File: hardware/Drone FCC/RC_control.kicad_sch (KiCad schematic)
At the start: 2 parts, among them J24 DSM Spektrum JST, J27 PPM Dupont

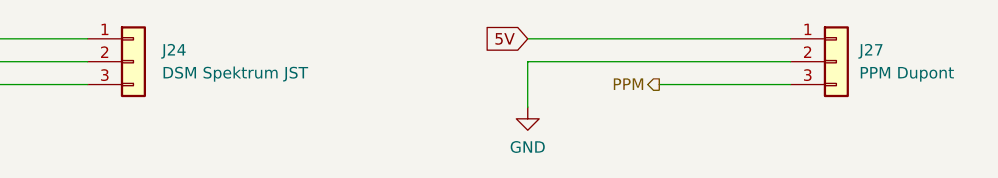
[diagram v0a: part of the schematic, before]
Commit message: re enumeration of components
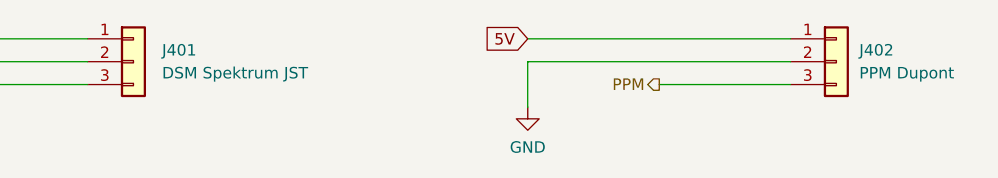
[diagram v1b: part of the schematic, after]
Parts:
- renumbered J24 to J401, J27 to J402
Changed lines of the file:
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@@
   (symbol (lib_id "Connector_Generic:Conn_01x03") (at 83.185 42.545 0) (unit 1)
     (in_bom yes) (on_board yes) (fields_autoplaced)
-    (property "Reference" "J24" (id 0) (at 86.36 41.2749 0)
+    (property "Reference" "J401" (id 0) (at 86.36 41.2749 0)
       (effects (font (size 1.27 1.27)) (justify left))
     )
@@
   (symbol (lib_id "Connector_Generic:Conn_01x03") (at 161.29 42.545 0) (unit 1)
     (in_bom yes) (on_board yes) (fields_autoplaced)
-    (property "Reference" "J27" (id 0) (at 163.83 41.2749 0)
+    (property "Reference" "J402" (id 0) (at 163.83 41.2749 0)
       (effects (font (size 1.27 1.27)) (justify left))
     )

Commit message: start routing
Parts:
- removed J401: DSM Spektrum JST, B3B-ZR-SM4-TF(LF)(SN):JST-B3B-ZR-SM4-TFLFSN-0-0-MFG, symbol Connector_Generic:Conn_01x03
- added J401: DSM Spektrum JST, B3B-ZR-SM4-TF(LF)(SN):JST-B3B-ZR-SM4-TFLFSN-0-0-MFG, symbol Connector_Generic:Conn_01x05
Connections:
- net 3V3: now also J401.1 (Pin_1)
- net DSM_DATA: now also J401.3 (Pin_3)
- net GND: now also J401.2 (Pin_2), J401.4 (Pin_4), J401.5 (Pin_5)
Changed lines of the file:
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@@
 (kicad_sch (version 20211123) (generator eeschema)
   (paper "A4")
+  (junction (at 48.895 50.165) (diameter 0) (color 0 0 0 0)
+  )
+  (junction (at 48.895 47.625) (diameter 0) (color 0 0 0 0)
+  )
+  (wire (pts (xy 48.895 47.625) (xy 48.895 50.165))
+    (stroke (width 0) (type default) (color 0 0 0 0))
+  )
+  (wire (pts (xy 48.895 50.165) (xy 48.895 52.705))
+    (stroke (width 0) (type default) (color 0 0 0 0))
+  )
   (wire (pts (xy 127 42.545) (xy 156.21 42.545))
+    (stroke (width 0) (type default) (color 0 0 0 0))
+  )
+  (wire (pts (xy 48.895 50.165) (xy 78.105 50.165))
     (stroke (width 0) (type default) (color 0 0 0 0))
   )
@@
   )
   (wire (pts (xy 48.895 40.005) (xy 78.105 40.005))
+    (stroke (width 0) (type default) (color 0 0 0 0))
+  )
+  (wire (pts (xy 48.895 47.625) (xy 78.105 47.625))
     (stroke (width 0) (type default) (color 0 0 0 0))
   )
@@
     (effects (font (size 1.27 1.27)) (justify right))
   )
-  (symbol (lib_id "Connector_Generic:Conn_01x03") (at 83.185 42.545 0) (unit 1)
+  (symbol (lib_id "Connector_Generic:Conn_01x05") (at 83.185 45.085 0) (unit 1)
     (in_bom yes) (on_board yes) (fields_autoplaced)
-    (property "Reference" "J401" (id 0) (at 86.36 41.2749 0)
+    (property "Reference" "J401" (id 0) (at 86.36 43.8149 0)
       (effects (font (size 1.27 1.27)) (justify left))
     )
-    (property "Value" "DSM Spektrum JST" (id 1) (at 86.36 43.8149 0)
+    (property "Value" "DSM Spektrum JST" (id 1) (at 86.36 46.3549 0)
       (effects (font (size 1.27 1.27)) (justify left))
     )
-    (property "Footprint" "B3B-ZR-SM4-TF(LF)(SN):JST-B3B-ZR-SM4-TFLFSN-0-0-MFG" (id 2) (at 83.185 42.545 0)
+    (property "Footprint" "B3B-ZR-SM4-TF(LF)(SN):JST-B3B-ZR-SM4-TFLFSN-0-0-MFG" (id 2) (at 83.185 45.085 0)
       (effects (font (size 1.27 1.27)) hide)
     )
-    (property "Datasheet" "~" (id 3) (at 83.185 42.545 0)
+    (property "Datasheet" "~" (id 3) (at 83.185 45.085 0)
       (effects (font (size 1.27 1.27)) hide)
     )
@@
     (pin "2")
     (pin "3")
+    (pin "4")
+    (pin "5")
   )
   (symbol (lib_id "Connector_Generic:Conn_01x03") (at 161.29 42.545 0) (unit 1)
@@
     (pin "1")
   )
-  (symbol (lib_id "power:GND") (at 48.895 47.625 0) (unit 1)
+  (symbol (lib_id "power:GND") (at 48.895 52.705 0) (unit 1)
     (in_bom yes) (on_board yes) (fields_autoplaced)
-    (property "Reference" "#PWR0119" (id 0) (at 48.895 53.975 0)
+    (property "Reference" "#PWR0119" (id 0) (at 48.895 59.055 0)
       (effects (font (size 1.27 1.27)) hide)
     )
-    (property "Value" "GND" (id 1) (at 48.895 52.07 0))
-    (property "Footprint" "" (id 2) (at 48.895 47.625 0)
+    (property "Value" "GND" (id 1) (at 48.895 57.15 0))
+    (property "Footprint" "" (id 2) (at 48.895 52.705 0)
       (effects (font (size 1.27 1.27)) hide)
     )
-    (property "Datasheet" "" (id 3) (at 48.895 47.625 0)
+    (property "Datasheet" "" (id 3) (at 48.895 52.705 0)
       (effects (font (size 1.27 1.27)) hide)
     )

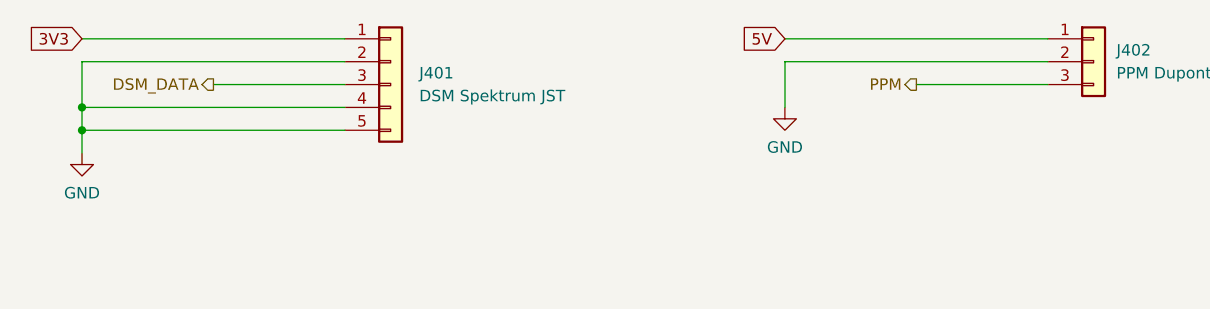
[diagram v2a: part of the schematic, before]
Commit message: add TVS diodes for SPI and ESD capacitors
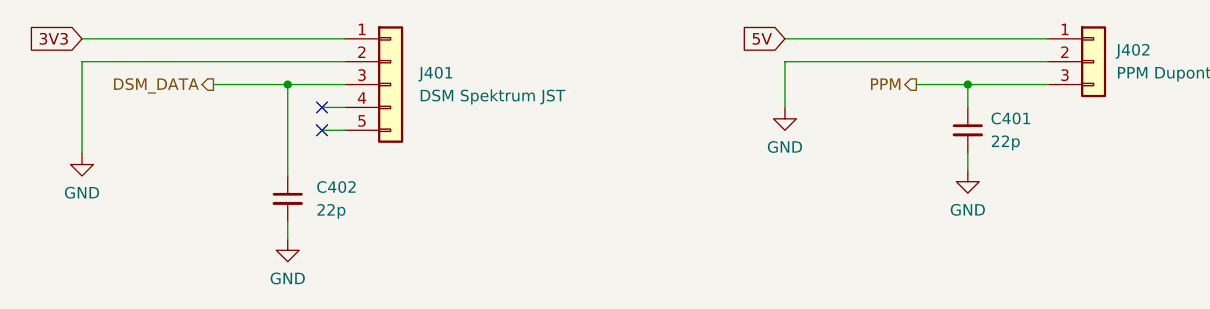
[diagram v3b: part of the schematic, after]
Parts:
- added C401, C402: 22p, Capacitor_SMD:C_0402_1005Metric_Pad0.74x0.62mm_HandSolder, symbol Device:C_Small
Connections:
- net DSM_DATA: now also C402.1
- net GND: now also C401.2, C402.2; no longer J401.4 (Pin_4), J401.5 (Pin_5)
- net PPM: now also C401.1
- no-connect marks 0 -> 2
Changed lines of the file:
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@@
 (kicad_sch (version 20211123) (generator eeschema)
   (paper "A4")
-  (junction (at 48.895 50.165) (diameter 0) (color 0 0 0 0)
-  )
-  (junction (at 48.895 47.625) (diameter 0) (color 0 0 0 0)
-  )
-  (wire (pts (xy 48.895 47.625) (xy 48.895 50.165))
-    (stroke (width 0) (type default) (color 0 0 0 0))
-  )
-  (wire (pts (xy 48.895 50.165) (xy 48.895 52.705))
+  (junction (at 71.755 45.085) (diameter 0) (color 0 0 0 0)
+  )
+  (junction (at 147.32 45.085) (diameter 0) (color 0 0 0 0)
+  )
+  (no_connect (at 75.565 50.165))
+  (no_connect (at 75.565 47.625))
+  (wire (pts (xy 48.895 42.545) (xy 48.895 52.705))
+    (stroke (width 0) (type default) (color 0 0 0 0))
+  )
+  (wire (pts (xy 75.565 50.165) (xy 78.105 50.165))
+    (stroke (width 0) (type default) (color 0 0 0 0))
+  )
+  (wire (pts (xy 147.32 52.705) (xy 147.32 54.61))
     (stroke (width 0) (type default) (color 0 0 0 0))
   )
@@
     (stroke (width 0) (type default) (color 0 0 0 0))
   )
-  (wire (pts (xy 48.895 50.165) (xy 78.105 50.165))
-    (stroke (width 0) (type default) (color 0 0 0 0))
-  )
   (wire (pts (xy 127 42.545) (xy 127 47.625))
     (stroke (width 0) (type default) (color 0 0 0 0))
@@
     (stroke (width 0) (type default) (color 0 0 0 0))
   )
-  (wire (pts (xy 48.895 47.625) (xy 78.105 47.625))
-    (stroke (width 0) (type default) (color 0 0 0 0))
-  )
-  (wire (pts (xy 48.895 42.545) (xy 48.895 47.625))
+  (wire (pts (xy 147.32 45.085) (xy 156.21 45.085))
+    (stroke (width 0) (type default) (color 0 0 0 0))
+  )
+  (wire (pts (xy 71.755 45.085) (xy 71.755 55.245))
     (stroke (width 0) (type default) (color 0 0 0 0))
   )
@@
     (stroke (width 0) (type default) (color 0 0 0 0))
   )
-  (wire (pts (xy 63.5 45.085) (xy 78.105 45.085))
-    (stroke (width 0) (type default) (color 0 0 0 0))
-  )
-  (wire (pts (xy 141.605 45.085) (xy 156.21 45.085))
+  (wire (pts (xy 71.755 60.325) (xy 71.755 62.23))
+    (stroke (width 0) (type default) (color 0 0 0 0))
+  )
+  (wire (pts (xy 63.5 45.085) (xy 71.755 45.085))
+    (stroke (width 0) (type default) (color 0 0 0 0))
+  )
+  (wire (pts (xy 141.605 45.085) (xy 147.32 45.085))
+    (stroke (width 0) (type default) (color 0 0 0 0))
+  )
+  (wire (pts (xy 75.565 47.625) (xy 78.105 47.625))
+    (stroke (width 0) (type default) (color 0 0 0 0))
+  )
+  (wire (pts (xy 147.32 45.085) (xy 147.32 47.625))
+    (stroke (width 0) (type default) (color 0 0 0 0))
+  )
+  (wire (pts (xy 71.755 45.085) (xy 78.105 45.085))
     (stroke (width 0) (type default) (color 0 0 0 0))
   )
@@
   (hierarchical_label "DSM_DATA" (shape output) (at 63.5 45.085 180)
     (effects (font (size 1.27 1.27)) (justify right))
+  )
+  (symbol (lib_id "power:GND") (at 147.32 54.61 0) (unit 1)
+    (in_bom yes) (on_board yes) (fields_autoplaced)
+    (property "Reference" "#PWR0192" (id 0) (at 147.32 60.96 0)
+      (effects (font (size 1.27 1.27)) hide)
+    )
+    (property "Value" "GND" (id 1) (at 147.32 59.055 0))
+    (property "Footprint" "" (id 2) (at 147.32 54.61 0)
+      (effects (font (size 1.27 1.27)) hide)
+    )
+    (property "Datasheet" "" (id 3) (at 147.32 54.61 0)
+      (effects (font (size 1.27 1.27)) hide)
+    )
+    (pin "1")
   )
   (symbol (lib_id "Connector_Generic:Conn_01x05") (at 83.185 45.085 0) (unit 1)
@@
     (pin "5")
   )
+  (symbol (lib_id "Device:C_Small") (at 147.32 50.165 0) (unit 1)
+    (in_bom yes) (on_board yes) (fields_autoplaced)
+    (property "Reference" "C401" (id 0) (at 149.86 48.9012 0)
+      (effects (font (size 1.27 1.27)) (justify left))
+    )
+    (property "Value" "22p" (id 1) (at 149.86 51.4412 0)
+      (effects (font (size 1.27 1.27)) (justify left))
+    )
+    (property "Footprint" "Capacitor_SMD:C_0402_1005Metric_Pad0.74x0.62mm_HandSolder" (id 2) (at 147.32 50.165 0)
+      (effects (font (size 1.27 1.27)) hide)
+    )
+    (property "Datasheet" "~" (id 3) (at 147.32 50.165 0)
+      (effects (font (size 1.27 1.27)) hide)
+    )
+    (pin "1")
+    (pin "2")
+  )
   (symbol (lib_id "Connector_Generic:Conn_01x03") (at 161.29 42.545 0) (unit 1)
     (in_bom yes) (on_board yes) (fields_autoplaced)
@@
     (pin "2")
     (pin "3")
+  )
+  (symbol (lib_id "Device:C_Small") (at 71.755 57.785 0) (unit 1)
+    (in_bom yes) (on_board yes) (fields_autoplaced)
+    (property "Reference" "C402" (id 0) (at 74.93 56.5212 0)
+      (effects (font (size 1.27 1.27)) (justify left))
+    )
+    (property "Value" "22p" (id 1) (at 74.93 59.0612 0)
+      (effects (font (size 1.27 1.27)) (justify left))
+    )
+    (property "Footprint" "Capacitor_SMD:C_0402_1005Metric_Pad0.74x0.62mm_HandSolder" (id 2) (at 71.755 57.785 0)
+      (effects (font (size 1.27 1.27)) hide)
+    )
+    (property "Datasheet" "~" (id 3) (at 71.755 57.785 0)
+      (effects (font (size 1.27 1.27)) hide)
+    )
+    (pin "1")
+    (pin "2")
   )
   (symbol (lib_id "power:GND") (at 127 47.625 0) (unit 1)
@@
       (effects (font (size 1.27 1.27)) hide)
     )
+    (pin "1")
+  )
+  (symbol (lib_id "power:GND") (at 71.755 62.23 0) (unit 1)
+    (in_bom yes) (on_board yes) (fields_autoplaced)
+    (property "Reference" "#PWR0193" (id 0) (at 71.755 68.58 0)
+      (effects (font (size 1.27 1.27)) hide)
+    )
+    (property "Value" "GND" (id 1) (at 71.755 66.675 0))
+    (property "Footprint" "" (id 2) (at 71.755 62.23 0)
+      (effects (font (size 1.27 1.27)) hide)
+    )
+    (property "Datasheet" "" (id 3) (at 71.755 62.23 0)
+      (effects (font (size 1.27 1.27)) hide)
+    )

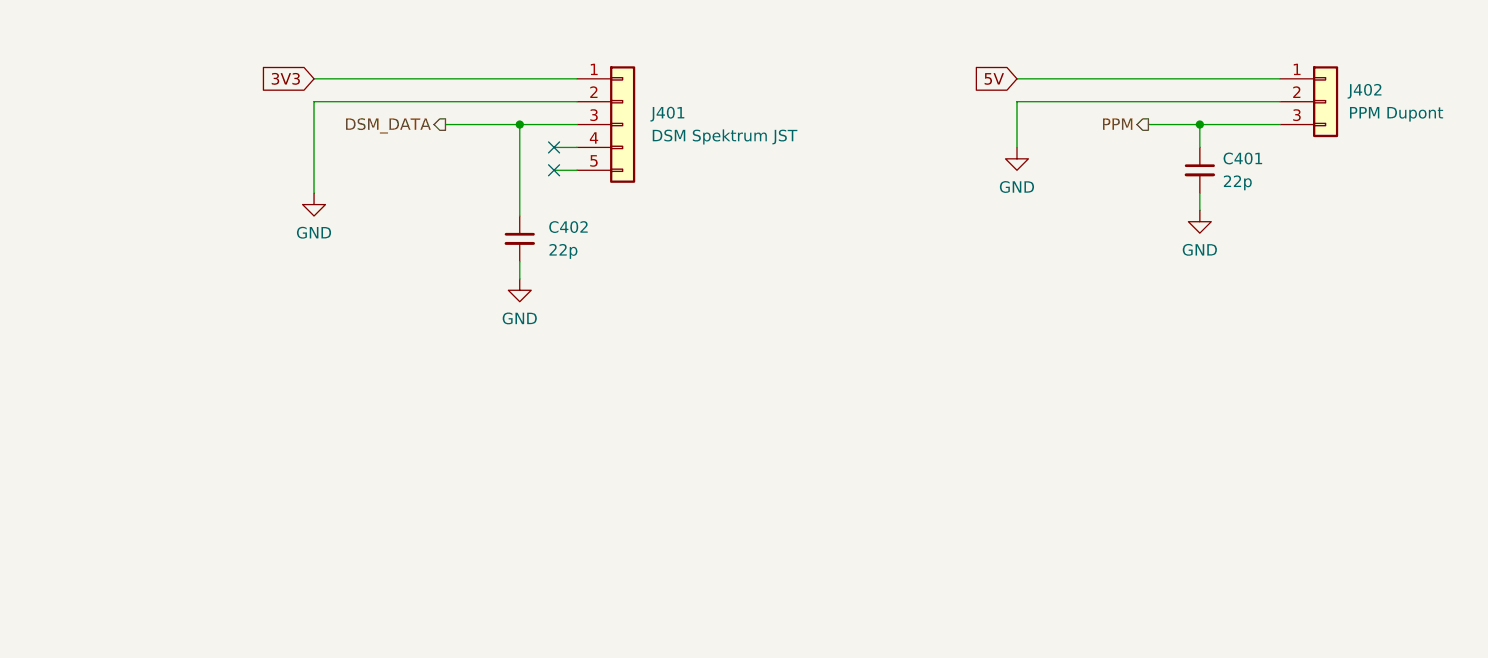
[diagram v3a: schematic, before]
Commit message: add TVS diodes for all the dupont pins
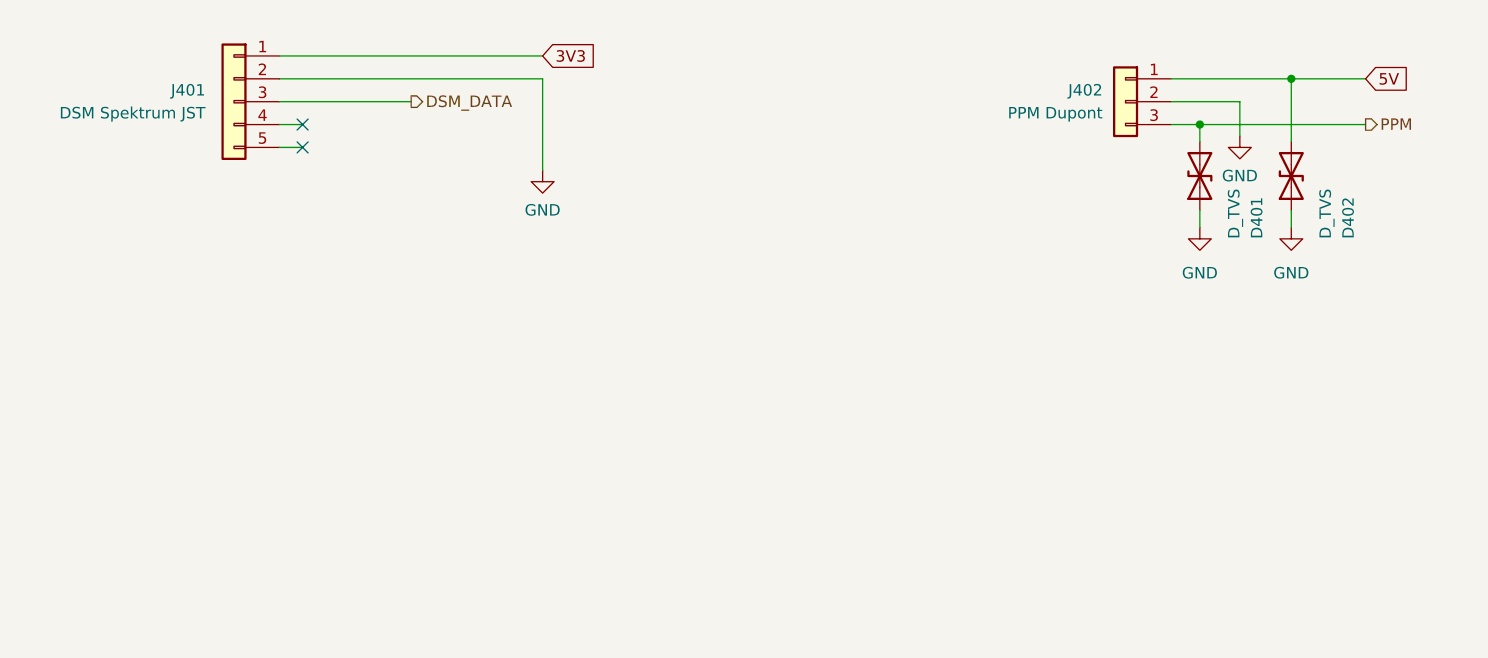
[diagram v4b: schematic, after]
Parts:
- removed C401, C402: 22p, Capacitor_SMD:C_0402_1005Metric_Pad0.74x0.62mm_HandSolder, symbol Device:C_Small
- added D401, D402: D_TVS, Diode_SMD:D_0402_1005Metric_Pad0.77x0.64mm_HandSolder, symbol Device:D_TVS
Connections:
- net 5V: now also D402.2 (A2)
- net GND: now also D401.1 (A1), D402.1 (A1)
- net PPM: now also D401.2 (A2)
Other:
- moved on the sheet: J401, J402

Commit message: added missing TVS diodes
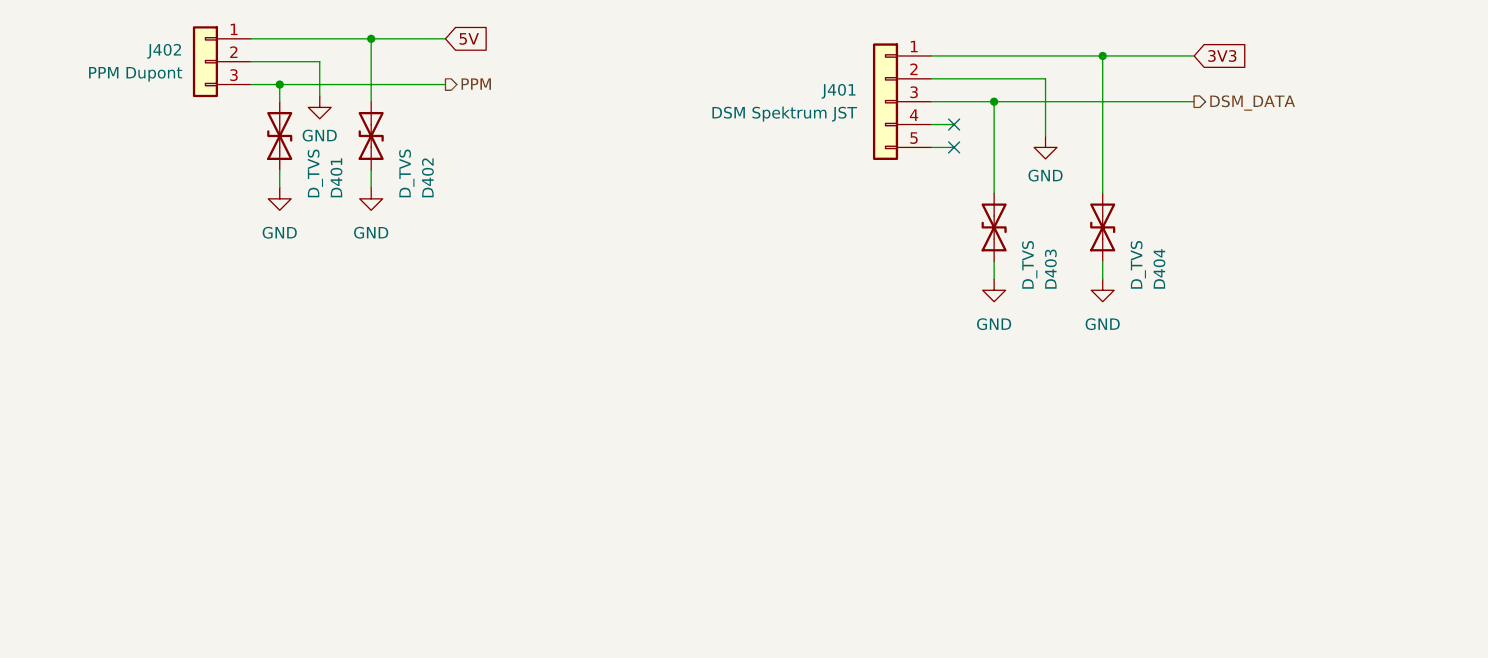
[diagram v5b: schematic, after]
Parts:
- added D403, D404: D_TVS, Diode_SMD:D_0402_1005Metric_Pad0.77x0.64mm_HandSolder, symbol Device:D_TVS
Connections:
- net 3V3: now also D404.2 (A2)
- net DSM_DATA: now also D403.2 (A2)
- net GND: now also D403.1 (A1), D404.1 (A1)
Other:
- moved on the sheet: D401, D402, J401, J402
